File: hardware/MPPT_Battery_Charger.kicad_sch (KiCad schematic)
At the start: 74 parts, among them Q24 SI7414DN-T1-E3, Q25 SI7414DN-T1-E3, Q5 SI2302DDS-T1-GE3, Q5 SI7414DN-T1-E3, Q6 SI7414DN-T1-E3, U22 BQ24650RVAT, U26 LMV321RIYLT, U28 LMV321RIYLT, U4 INA199C1DCKR

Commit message: commit
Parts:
- removed R200: 25m, symbol Device:R_US
- removed R202 (x2): 10R, symbol Device:R_US
- removed R207: 33m, symbol Device:R_US
- removed R209: 5.23k, symbol Device:R_US
- removed R224: 8.2k, symbol Device:R_US
- removed R31 (x2), R36: 10k, symbol Device:R_US
- added R207: 33m, footprints:WSL2512R0330FEA18, symbol WSL2512R0330FEA18:RES
- added R209: 5.23k, footprints:CRCW06035K23FKEAHP, symbol CRCW06035K23FKEAHP:RES
- added R36 (x3): 10k, footprints:RC0805FR-0710KL, symbol RC0805FR-0710KL:RES
- added R58: 25m, footprints:WSL2010R0250FEA18, symbol WSL2010R0250FEA18:WSL2010R0250FEA18
- added R59, R60: 10R, footprints:CRCW060310R0FKEAHP, symbol CRCW060310R0FKEAHP:CRCW060310R0FKEAHP
- added R72: 8.2k, footprints:CRCW06038K20FKEAHP, symbol CRCW06038K20FKEAHP:RES
- R207: footprint (none) -> footprints:WSL2512R0330FEA18; symbol Device:R_US -> WSL2512R0330FEA18:RES
- R208: footprint (none) -> footprints:WSL2010R0200FEA; symbol Device:R_US -> WSL2010R0200FEA:WSL2010R0200FEA; Arrow Part Number (none) -> WSL2010R0200FEA; Arrow Price/Stock (none) -> https://www.arrow.com/en/products/wsl2010r0200fea/vishay; Manufacturer_Name (none) -> Vishay; Manufacturer_Part_Number (none) -> WSL2010R0200FEA; Mouser Part Number (none) -> 71-WSL2010R0200FEA; Mouser Price/Stock (none) -> https://www.mouser.co.uk/ProductDetail/Vishay-Dale/WSL2010R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
- R209: footprint (none) -> footprints:CRCW06035K23FKEAHP; symbol Device:R_US -> CRCW06035K23FKEAHP:RES
- R221: footprint (none) -> footprints:CRCW060330K0FKEAHP; symbol Device:R_US -> CRCW060330K0FKEAHP:RES
- R222: footprint (none) -> footprints:CRCW060324K0FKEAHP; symbol Device:R_US -> CRCW060324K0FKEAHP:RES
- R225: footprint (none) -> footprints:CRCW06037K50FKEAHP; symbol Device:R_US -> CRCW06037K50FKEAHP:CRCW06037K50FKEAHP; automotive (none) -> Yes; automotive grade (none) -> Grade 0; category (none) -> Res; composition (none) -> Thick Film; device class L1 (none) -> Passive Components; device class L2 (none) -> Resistors; device class L3 (none) -> Chip SMD Resistors; height (none) -> 0.55mm; ipc land pattern name (none) -> RESC16085X45; lead free (none) -> Yes; library id (none) -> ac0eb7131481e5d0; manufacturer (none) -> Vishay; package (none) -> 0603; power (none) -> 250mW; power rating (none) -> 0.33W; resistance (none) -> 7.5kΩ; rohs (none) -> Yes; series (none) -> CRCW-HP e3; temperature coefficient (none) -> 100ppm/°C; temperature range high (none) -> +155°C; temperature range low (none) -> -55°C; tolerance (none) -> 1%; voltage rating (none) -> 75V
- R36: footprint (none) -> footprints:RC0805FR-0710KL; symbol Device:R_US -> RC0805FR-0710KL:RES
- R38: footprint (none) -> footprints:CRCW0603100KFKEAHP; symbol Device:R_US -> CRCW0603100KFKEAHP:CRCW0603100KFKEAHP; Arrow Part Number (none) -> CRCW0603100KFKEAHP; Arrow Price/Stock (none) -> https://www.arrow.com/en/products/crcw0603100kfkeahp/vishay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; Height (none) -> 0.55; Manufacturer_Name (none) -> Vishay; Manufacturer_Part_Number (none) -> CRCW0603100KFKEAHP; Mouser Part Number (none) -> 71-CRCW0603100KFKEAH; Mouser Price/Stock (none) -> https://www.mouser.co.uk/ProductDetail/Vishay-Dale/CRCW0603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
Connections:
- net BC_A_TS: now also R209.1; no longer R209.2
- net BC_A_~{EN}: now also R38.2; no longer R38.1
- net BC_B_TS: now also R209.1
- net BC_B_~{EN}: now also R38.2; no longer R38.1
- net GND: now also R38.1, R38.1, R72.1; no longer R38.2, R38.2
- net VBC_IN: now also R36.1, R36.1, R36.1, R36.1; no longer R36.2
- net VBC_N: now also R221.2, R58.1; no longer R221.1
- net VBC_OUT: now also R207.1, R208.1, R207.1; no longer R207.2, R208.2
- net VCC1: now also R60.1
- net VCC2: now also R59.1
- net VIN: now also R208.2; no longer R208.1
- net VPANELS: now also R58.2
- net VREF1: now also R209.2; no longer R209.1
- net at C200.1, C201.1, D3.3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: now also R59.2
- net at C11.1, L200.2, U22.10 (SRP): now also R207.2; no longer R207.1
- net at C200.1, C201.1, D3.3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: now also R60.2
- net at D2.2 (A): now also R36.2; no longer R36.1
- net at C11.1, L200.2, U22.10 (SRP): now also R207.2
- net at D1.2 (A): now also R36.2 (x2)
- net at U28.3 (+): now also R221.1, R72.2; no longer R221.2
- net at D2.2 (A): now also R36.2
- net at U22.7 (TERM_EN): now also R209.2
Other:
- moved on the sheet: R207, R208, R209, R221, R222, R225, R36, R38

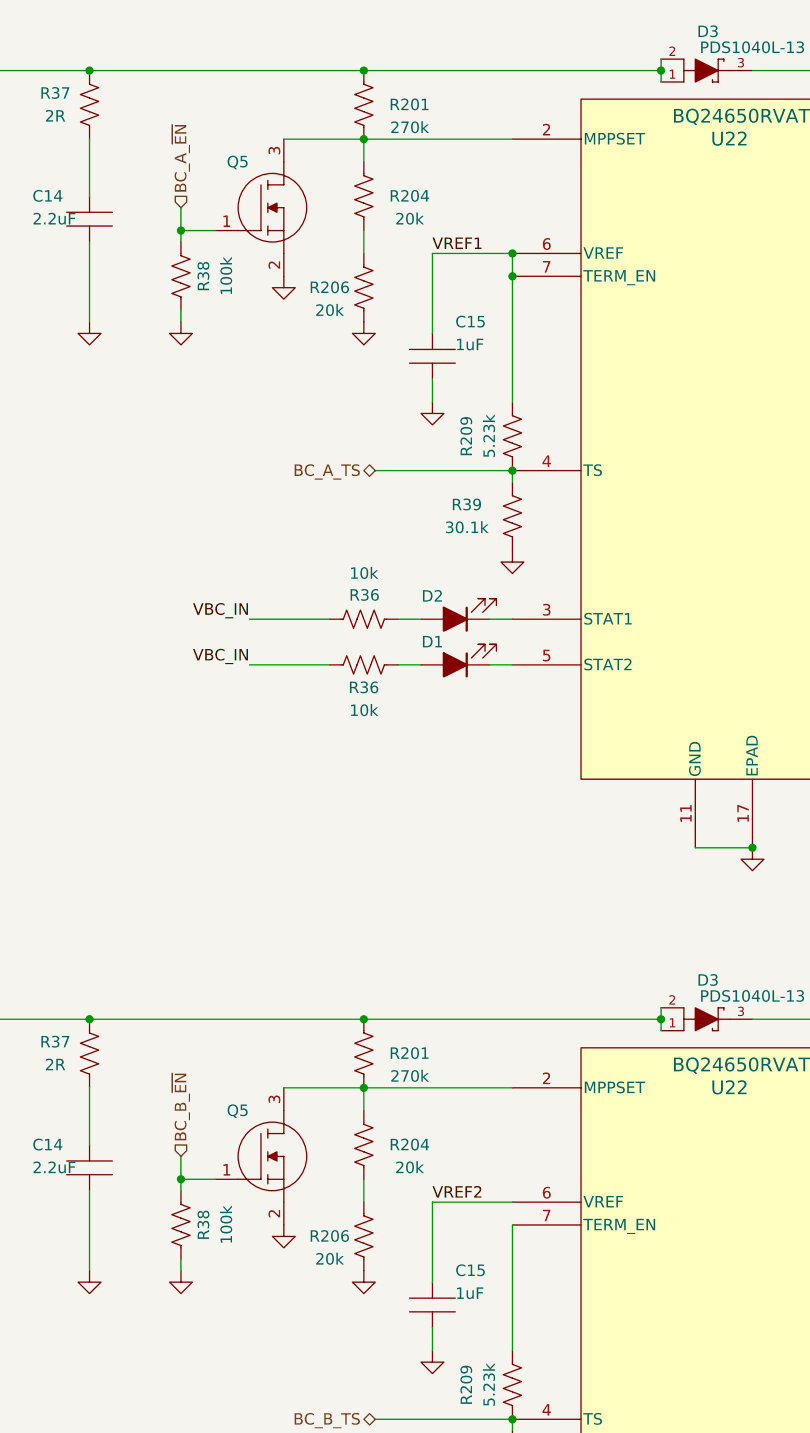
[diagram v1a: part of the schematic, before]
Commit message: hardware: update in footprints
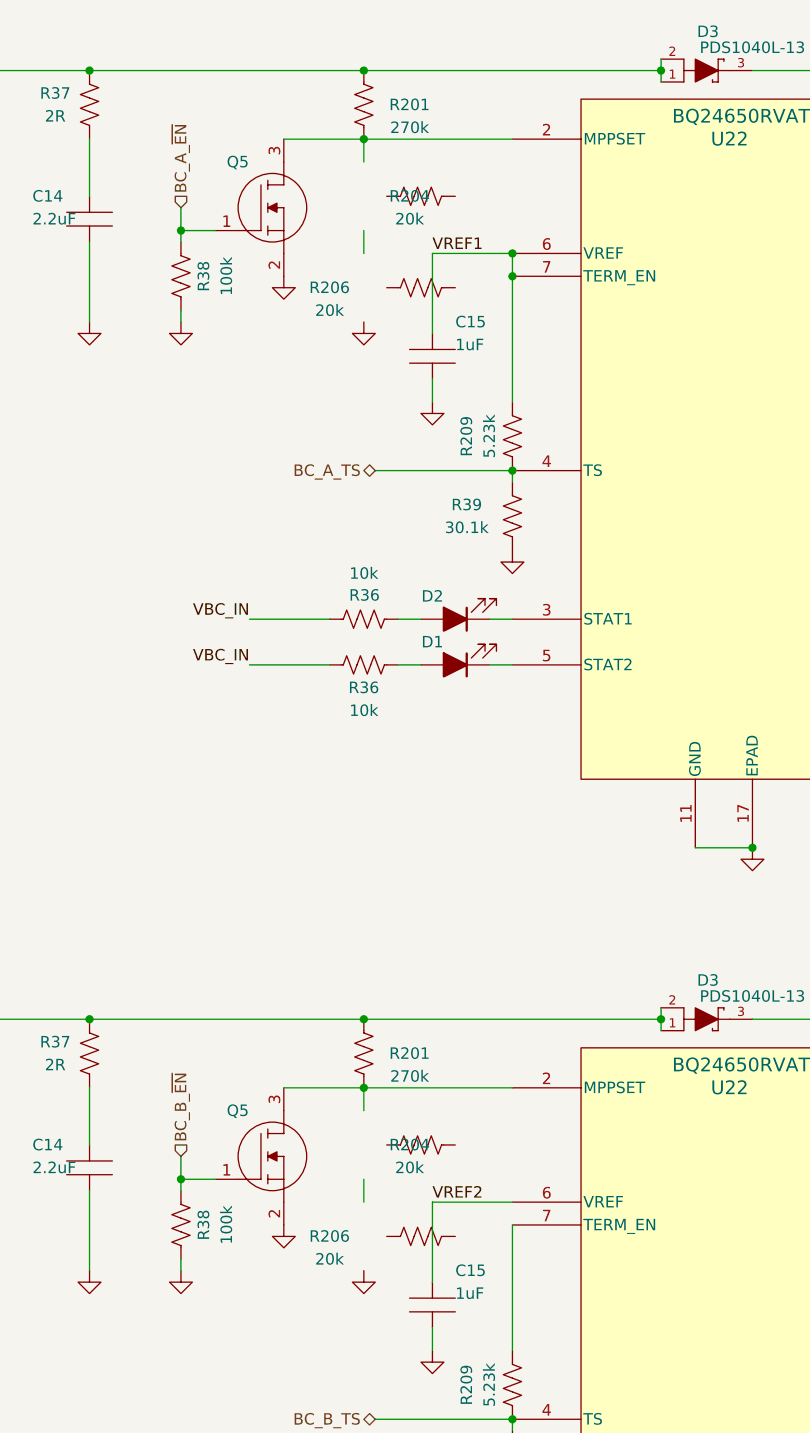
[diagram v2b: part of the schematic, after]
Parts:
- R204, R206: footprint (none) -> footprints:CRCW060320K0FKEAHP; symbol Device:R_US -> CRCW060320K0FKEAHP:CRCW060320K0FKEAHP; automotive (none) -> Yes; automotive grade (none) -> Grade 0; category (none) -> Res; composition (none) -> Thick Film; device class L1 (none) -> Passive Components; device class L2 (none) -> Resistors; device class L3 (none) -> Chip SMD Resistors; height (none) -> 0.55mm; ipc land pattern name (none) -> RESC16085X45; lead free (none) -> Yes; library id (none) -> 6d0e00b833a89e4b; manufacturer (none) -> Vishay; package (none) -> 0603; power (none) -> 250mW; power rating (none) -> 0.33W; resistance (none) -> 20kΩ; rohs (none) -> Yes; series (none) -> CRCW-HP e3; temperature coefficient (none) -> 100ppm/°C; temperature range high (none) -> +155°C; temperature range low (none) -> -55°C; tolerance (none) -> 1%; voltage rating (none) -> 75V
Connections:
- net GND: no longer R206.2, R206.2
- net at Q5.3 (D), R201.2, U22.2 (MPPSET): no longer R204.1 (x2)
- net at R204.2: no longer R206.1 (x2)
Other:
- moved on the sheet: R204, R206

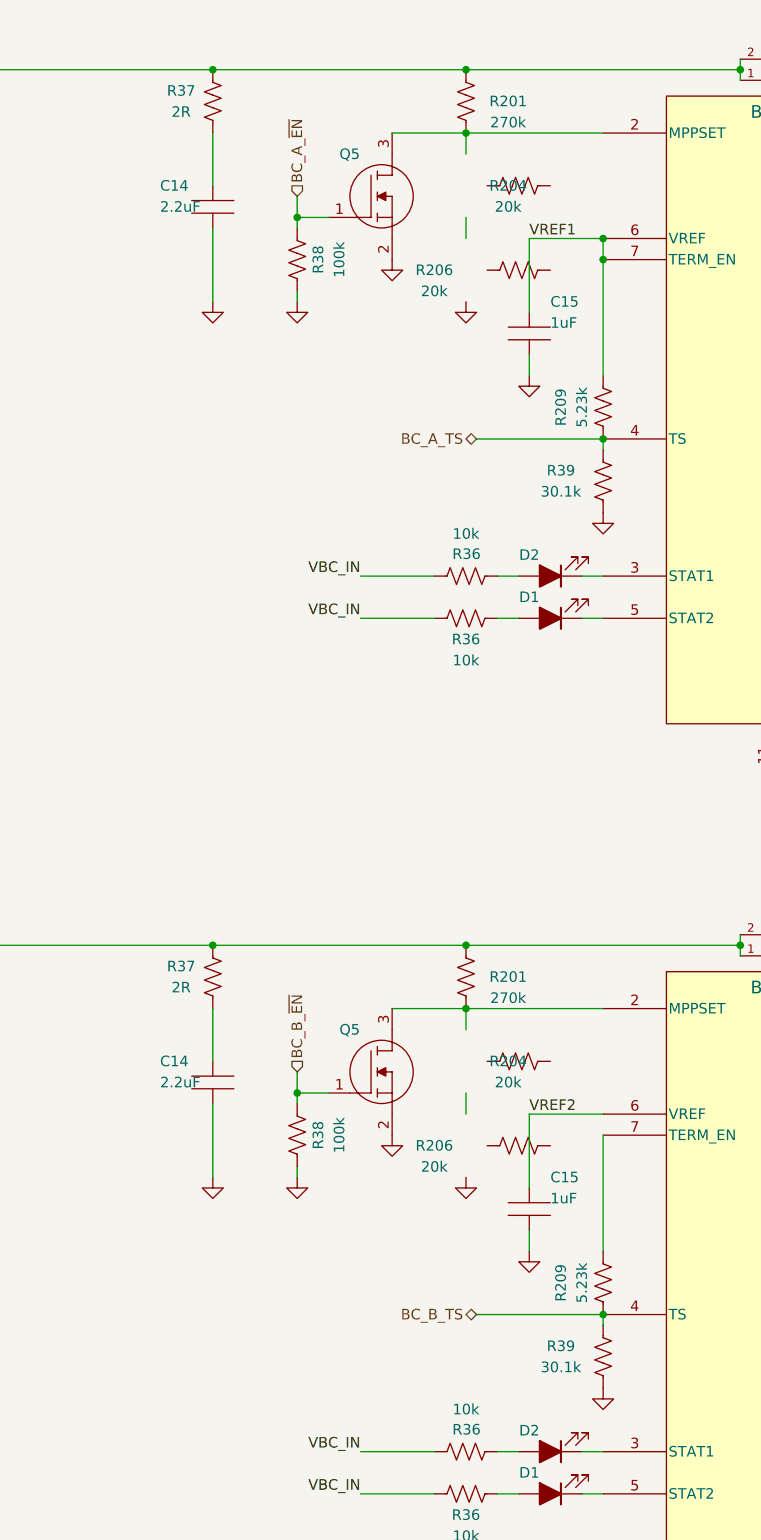
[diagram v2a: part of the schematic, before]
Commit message: hardware: Almost all the resistores were added.
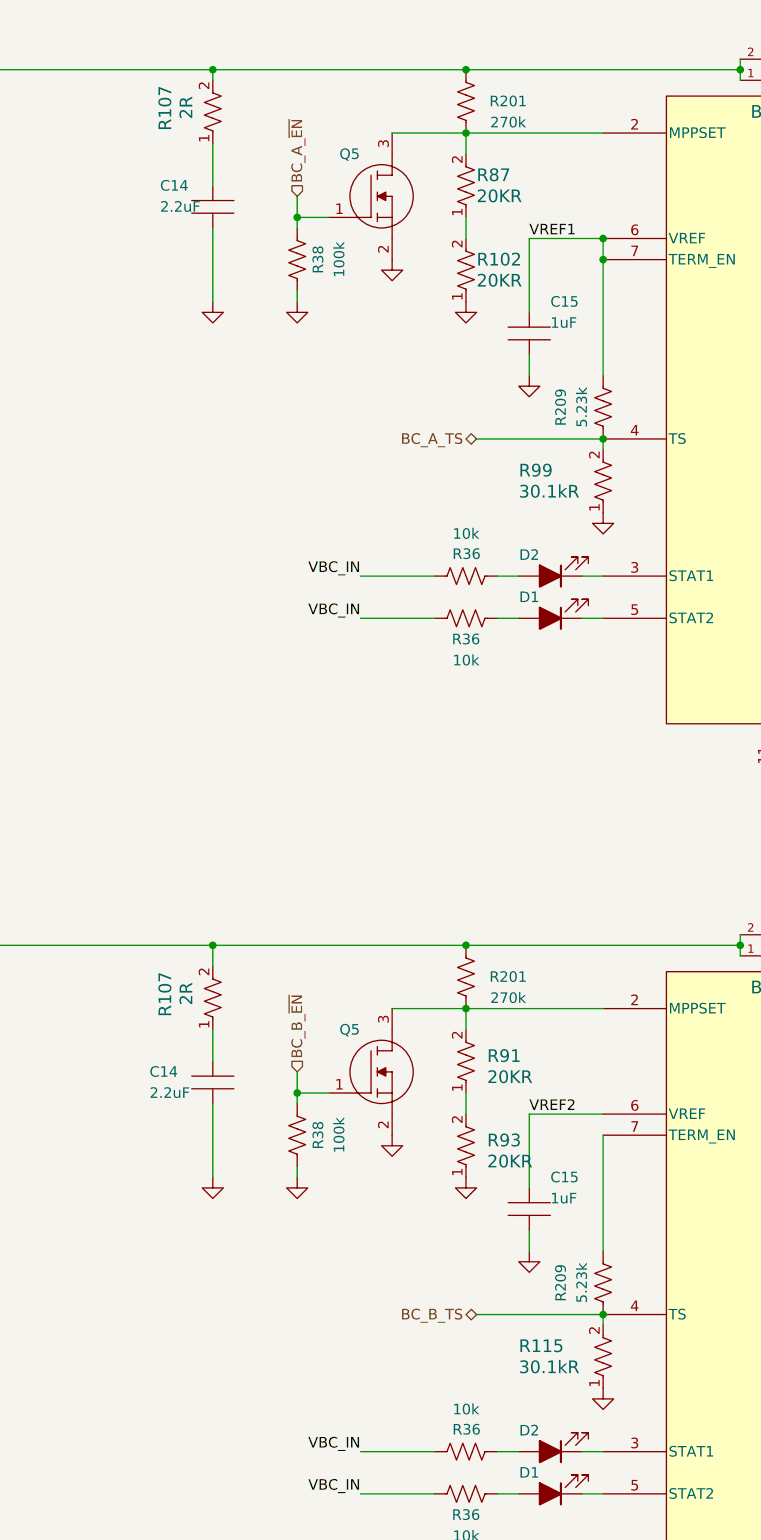
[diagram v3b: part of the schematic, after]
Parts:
- removed R204 (x2), R206 (x2): 20k, footprints:CRCW060320K0FKEAHP, symbol CRCW060320K0FKEAHP:CRCW060320K0FKEAHP
- removed R37 (x2): 2R, symbol Device:R_US
- removed R39 (x2): 30.1k, symbol Device:R_US
- added R102, R87, R91, R93: 20KR, RES_CRCW_0805_VIS, symbol CRCW080520K0FKEAHP:CRCW080520K0FKEAHP
- added R107 (x2): 2R, RC2010N_VIS, symbol CRCW20102R00FKEF:CRCW20102R00FKEF
- added R115, R99: 30.1kR, RES_CRCW_0603_VIS, symbol CRCW060330K1FKEAHP:CRCW060330K1FKEAHP
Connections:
- net BC_A_TS: now also R99.2
- net BC_B_TS: now also R115.2
- net GND: now also R102.1, R115.1, R93.1, R99.1
- net VBC_N: now also R107.2, R107.2
- net at C14.1: now also R107.1 (x2)
- net at Q5.3 (D), R201.2, U22.2 (MPPSET): now also R87.2
- net at Q5.3 (D), R201.2, U22.2 (MPPSET): now also R91.2
- new net: R102.2, R87.1
- new net: R91.1, R93.2
